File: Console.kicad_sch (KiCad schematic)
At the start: 37 parts, among them J1 SWD CONN, J2 Conn_01x08_Female, J3 Micro_SD_Card, J4 USB_B_Micro, J5 Conn_01x08_Female, U1 LM1117MPX-3_3_NOPB, U2 STM32F103TBUx

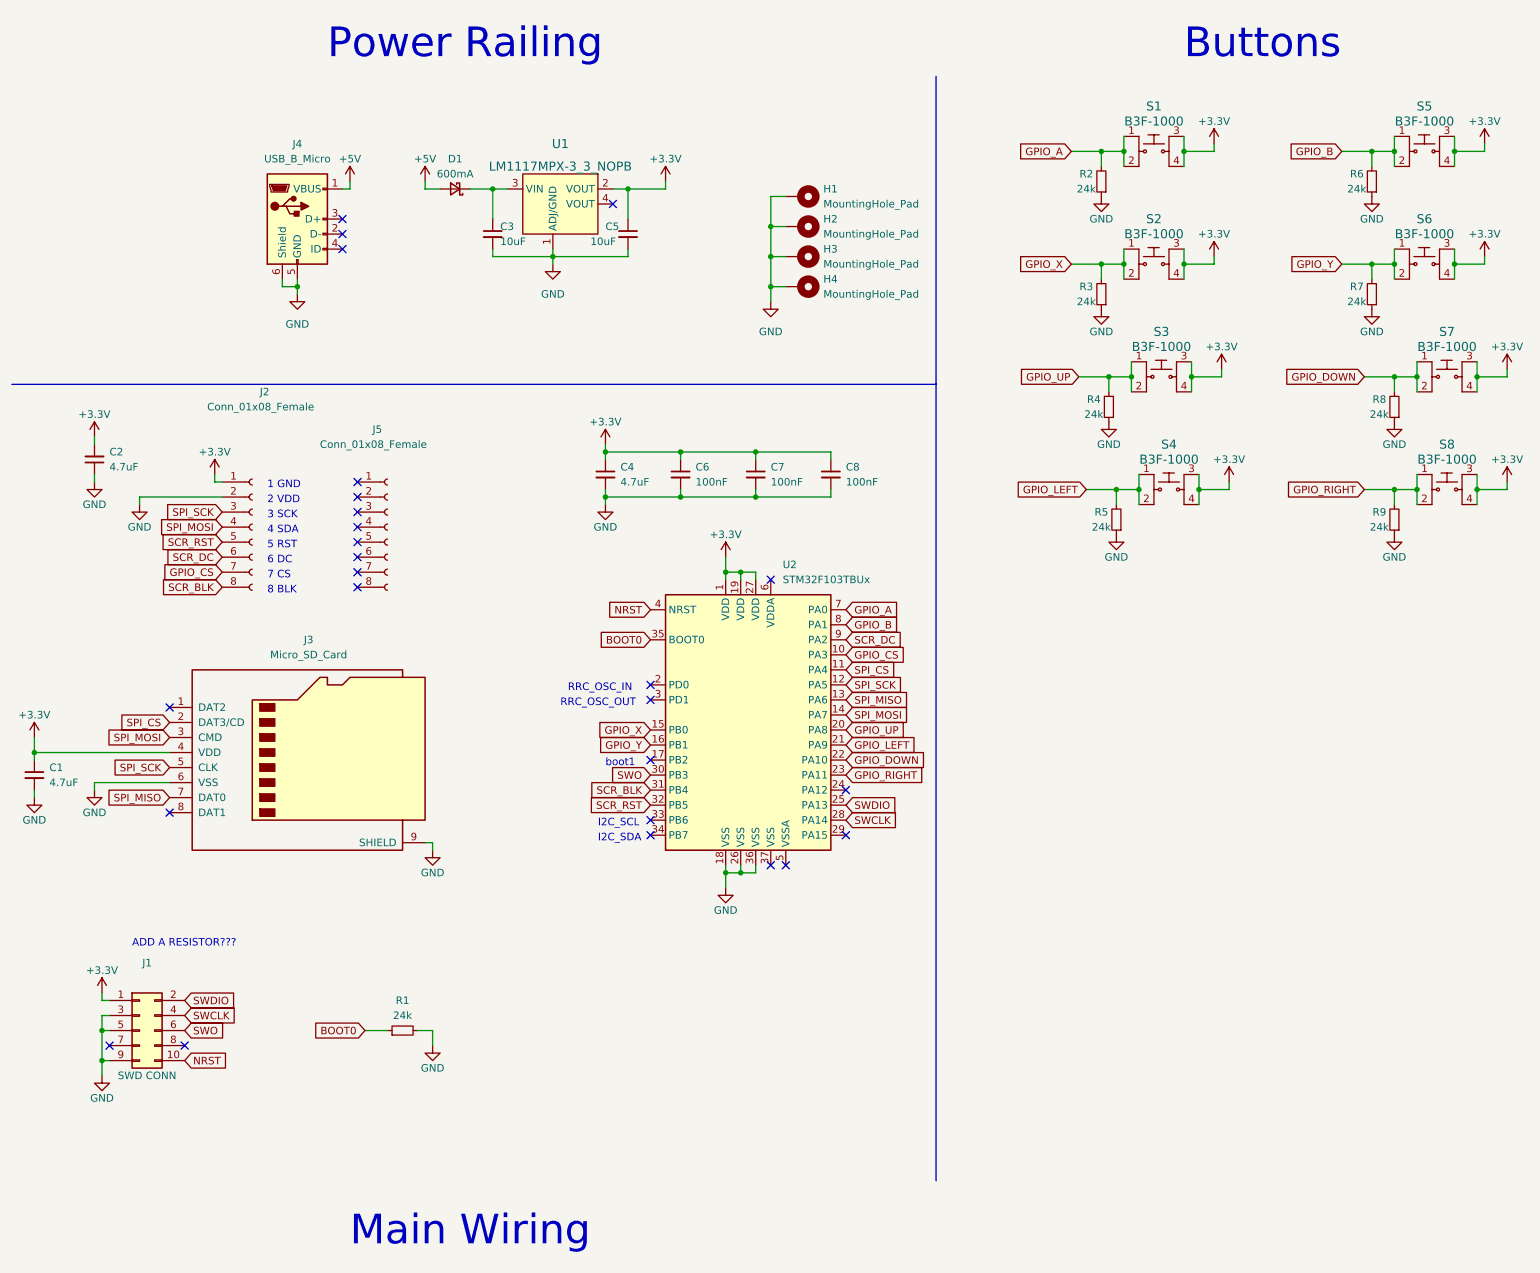
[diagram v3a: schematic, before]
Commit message: fixed problems, switched MCU with another of the same product line
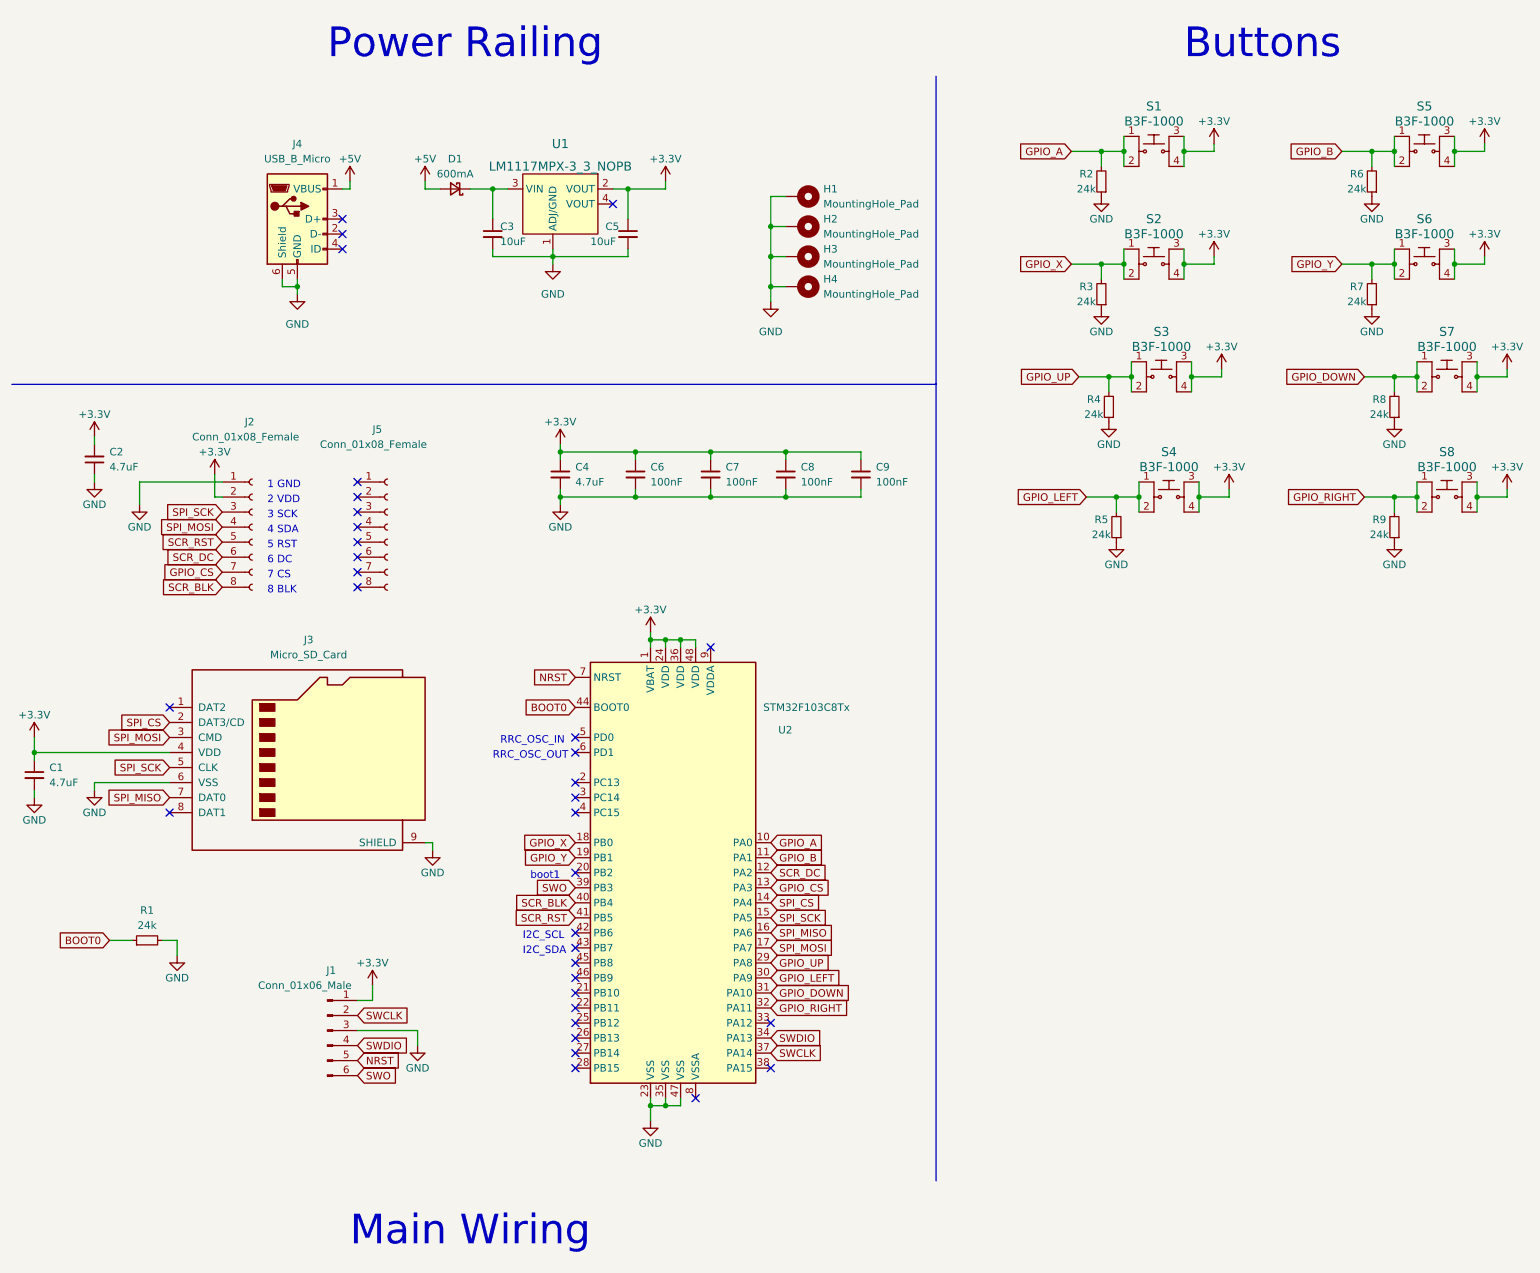
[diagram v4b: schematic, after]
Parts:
- removed J1: SWD CONN, Connector_PinHeader_1.27mm:PinHeader_2x05_P1.27mm_Vertical_SMD, symbol Connector_Generic:Conn_02x05_Odd_Even
- removed U2: STM32F103TBUx, Package_DFN_QFN:QFN-36-1EP_6x6mm_P0.5mm_EP4.1x4.1mm, symbol MCU_ST_STM32F1:STM32F103TBUx
- added C9: 100nF, Capacitor_SMD:C_0402_1005Metric, symbol Device:C_Small
- added J1: Conn_01x06_Male, Connector_PinHeader_2.54mm:PinHeader_1x06_P2.54mm_Vertical, symbol Connector:Conn_01x06_Male
- added U2: STM32F103C8Tx, Package_QFP:LQFP-48_7x7mm_P0.5mm, symbol MCU_ST_STM32F1:STM32F103C8Tx
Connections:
- net +3.3V: now also J2.2 (Pin_2), C9.1, J1.1 (Pin_1), U2.1 (VBAT), U2.24 (VDD), U2.36 (VDD), U2.48 (VDD); no longer J2.1 (Pin_1)
- net BOOT0: now also U2.44 (BOOT0)
- net GND: now also J2.1 (Pin_1), C9.2, J1.3 (Pin_3), U2.23 (VSS), U2.35 (VSS), U2.47 (VSS); no longer J2.2 (Pin_2)
- net GPIO_A: now also U2.10 (PA0)
- net GPIO_B: now also U2.11 (PA1)
- net GPIO_CS: now also U2.13 (PA3)
- net GPIO_DOWN: now also U2.31 (PA10)
- net GPIO_LEFT: now also U2.30 (PA9)
- net GPIO_RIGHT: now also U2.32 (PA11)
- net GPIO_UP: now also U2.29 (PA8)
- net GPIO_X: now also U2.18 (PB0)
- net GPIO_Y: now also U2.19 (PB1)
- net NRST: now also J1.5 (Pin_5), U2.7 (NRST)
- net SCR_BLK: now also U2.40 (PB4)
- net SCR_DC: now also U2.12 (PA2)
- net SCR_RST: now also U2.41 (PB5)
- net SPI_CS: now also U2.14 (PA4)
- net SPI_MISO: now also U2.16 (PA6)
- net SPI_MOSI: now also U2.17 (PA7)
- net SPI_SCK: now also U2.15 (PA5)
- net SWCLK: now also J1.2 (Pin_2), U2.37 (PA14)
- net SWDIO: now also J1.4 (Pin_4), U2.34 (PA13)
- net SWO: now also J1.6 (Pin_6), U2.39 (PB3)
- no-connect marks 26 -> 34
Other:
- note removed: "ADD A RESISTOR???"
- moved on the sheet: C4, C6, C7, C8, R1, R5, R9, S4, S8
